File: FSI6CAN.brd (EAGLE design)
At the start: 35 x 49 mm, 39 parts, among them IC2 TCAN332DR, IC3 ATMEGA328P, IC4 MCP2515

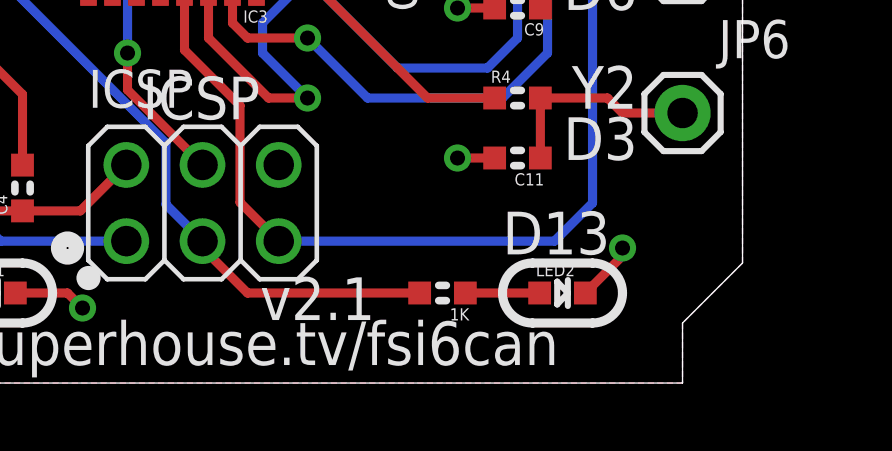
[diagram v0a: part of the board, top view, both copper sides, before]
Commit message: Fixed value of R10
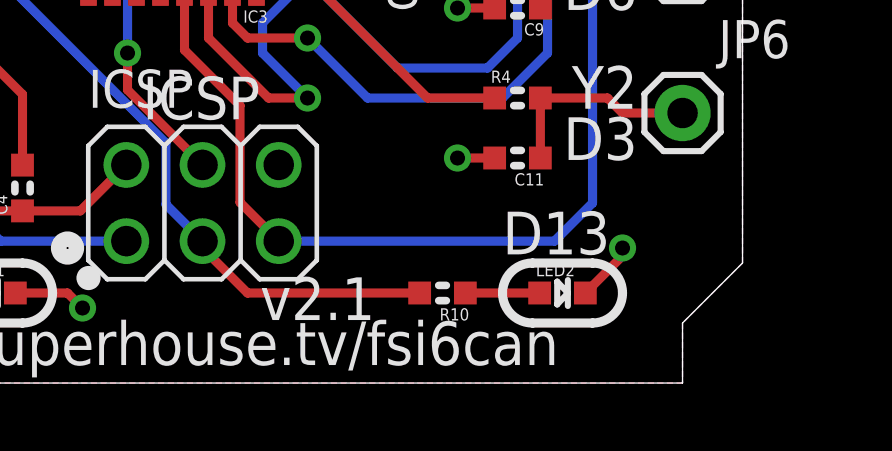
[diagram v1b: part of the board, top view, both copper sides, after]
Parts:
- renumbered 1K to R10
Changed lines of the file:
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@@
 <?xml version="1.0" encoding="utf-8"?>
 <!DOCTYPE eagle SYSTEM "eagle.dtd">
-<eagle version="9.5.0">
+<eagle version="9.5.2">
 <drawing>
 <settings>
@@
 <attribute name="VALUE" x="27.484" y="3.6348" size="1.016" layer="27"/>
 </element>
-<element name="1K" library="SuperHouse-DiscreteSemi" library_urn="urn:adsk.eagle:library:11768461" package="R0603" package3d_urn="urn:adsk.eagle:package:11768543/2" value="1K" x="25" y="3" smashed="yes" rot="R180">
+<element name="R10" library="SuperHouse-DiscreteSemi" library_urn="urn:adsk.eagle:library:11768461" package="R0603" package3d_urn="urn:adsk.eagle:package:11768543/2" value="1K" x="25" y="3" smashed="yes" rot="R180">
 <attribute name="NAME" x="25.889" y="2.492" size="0.4064" layer="25" font="vector" rot="R180"/>
 <attribute name="VALUE" x="24.084" y="3.6348" size="1.016" layer="27" font="vector"/>
@@
 <signal name="N$1">
 <contactref element="LED2" pad="A"/>
-<contactref element="1K" pad="1"/>
+<contactref element="R10" pad="1"/>
 <wire x1="28.238" y1="3" x2="25.762" y2="3" width="0.3048" layer="1"/>
 </signal>
@@
 <wire x1="18.5" y1="3" x2="17" y2="4.5" width="0.3048" layer="1"/>
 <wire x1="17" y1="4.5" x2="17" y2="4.73" width="0.3048" layer="1"/>
-<contactref element="1K" pad="2"/>
+<contactref element="R10" pad="2"/>
 <wire x1="24.238" y1="3" x2="18.5" y2="3" width="0.3048" layer="1"/>
 <wire x1="11.7074" y1="20.3" x2="11.7074" y2="21.5" width="0.3048" layer="1"/>
